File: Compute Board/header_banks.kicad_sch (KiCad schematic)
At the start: 12 parts, among them J3 Conn_01x02, J4 Conn_02x06_Top_Bottom, J5 Conn_02x08_Counter_Clockwise, J6 Conn_01x06, J7 Conn_01x07, J8 Conn_01x05, J9 Conn_01x08

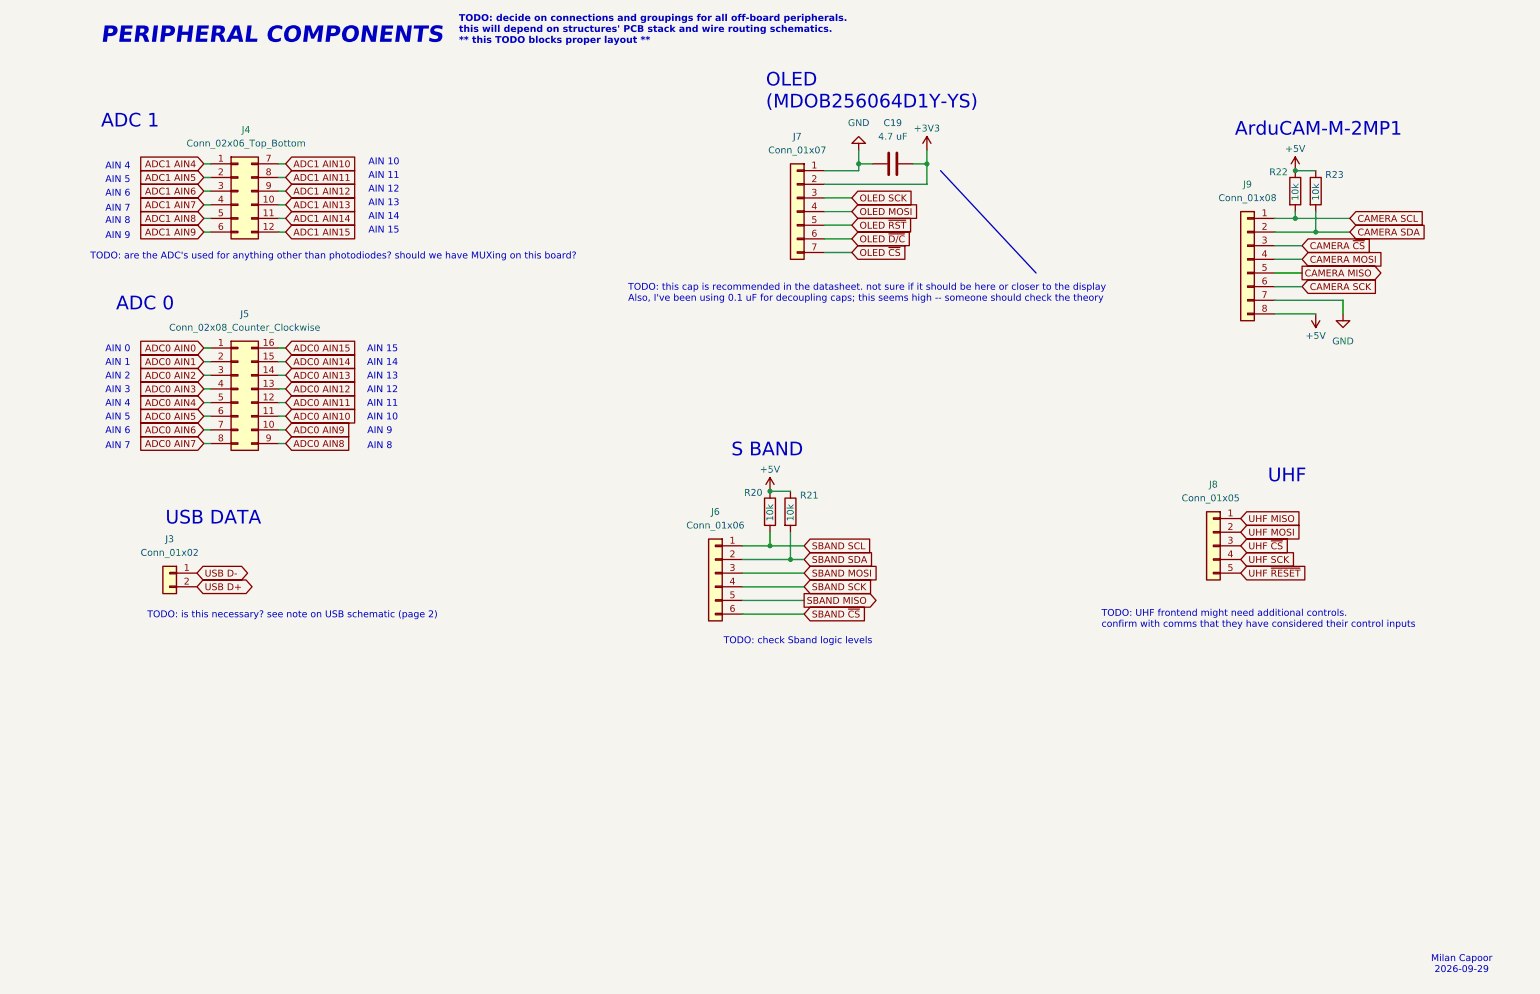
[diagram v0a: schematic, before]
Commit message: Push layout-ready schematics and partial routing
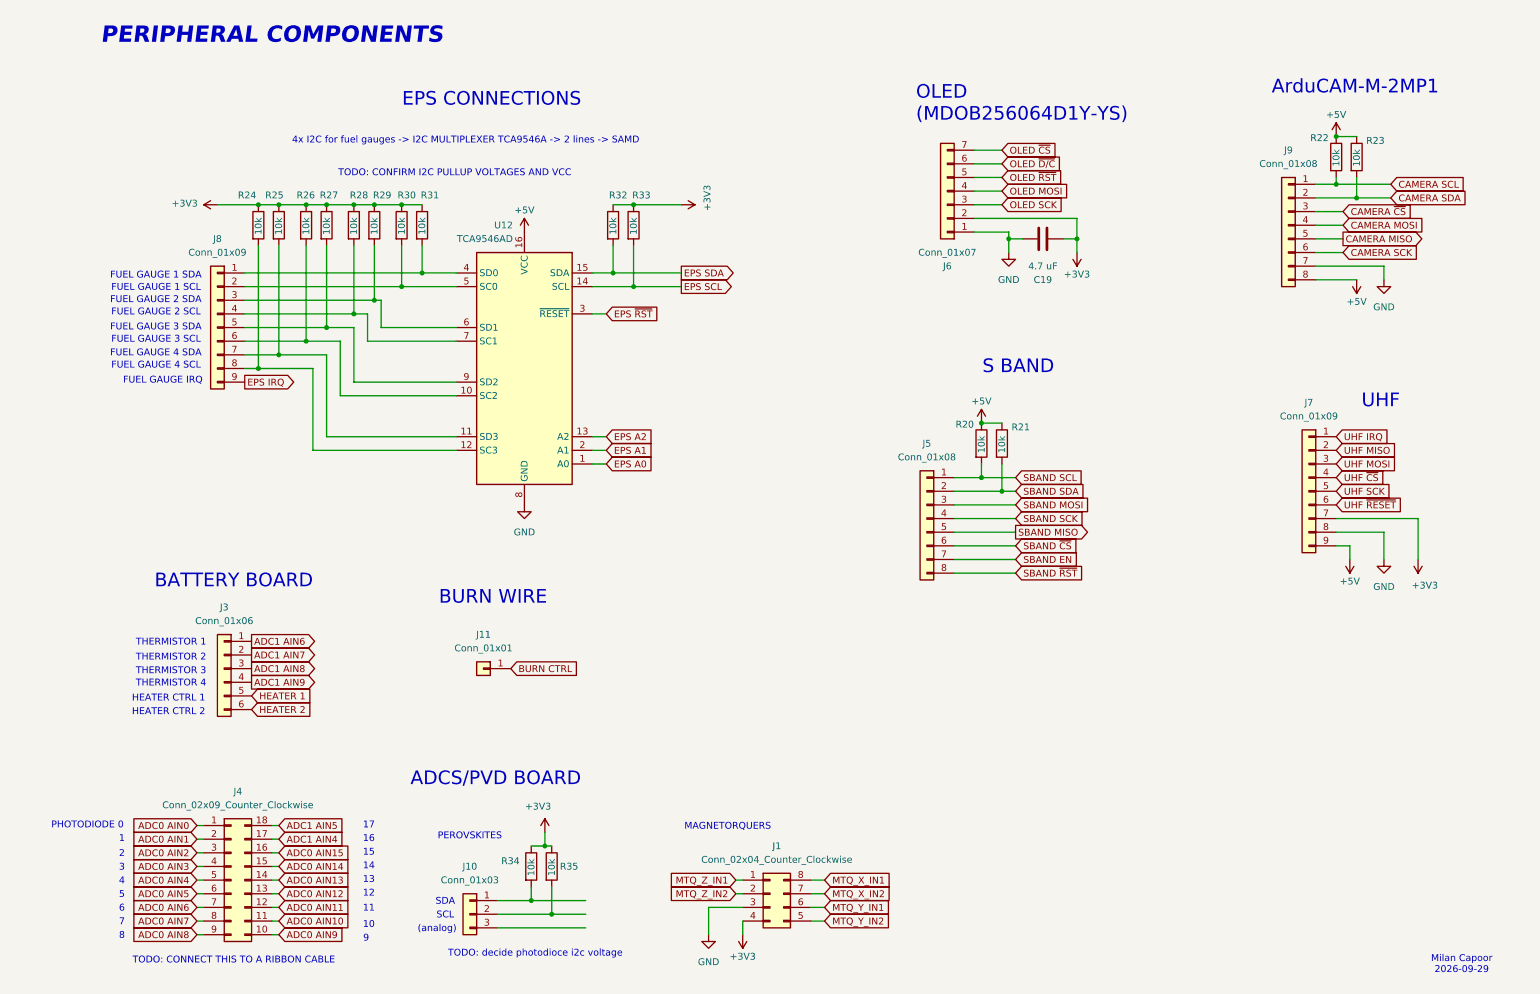
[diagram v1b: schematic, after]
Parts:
- removed J3: Conn_01x02, Connector_PinSocket_2.54mm:PinSocket_1x02_P2.54mm_Vertical, symbol Connector_Generic:Conn_01x02
- removed J4: Conn_02x06_Top_Bottom, Connector_PinSocket_2.54mm:PinSocket_2x06_P2.54mm_Vertical, symbol Connector_Generic:Conn_02x06_Top_Bottom
- removed J5: Conn_02x08_Counter_Clockwise, Connector_PinSocket_2.54mm:PinSocket_2x08_P2.54mm_Vertical, symbol Connector_Generic:Conn_02x08_Counter_Clockwise
- removed J6: Conn_01x06, Connector_PinSocket_2.54mm:PinSocket_1x06_P2.54mm_Vertical, symbol Connector_Generic:Conn_01x06
- removed J7: Conn_01x07, Connector_PinSocket_2.54mm:PinSocket_1x07_P2.54mm_Vertical, symbol Connector_Generic:Conn_01x07
- removed J8: Conn_01x05, Connector_PinSocket_2.54mm:PinSocket_1x05_P2.54mm_Vertical, symbol Connector_Generic:Conn_01x05
- added J1: Conn_02x04_Counter_Clockwise, Connector_PinSocket_2.54mm:PinSocket_2x04_P2.54mm_Vertical, symbol Connector_Generic:Conn_02x04_Counter_Clockwise
- added J10: Conn_01x03, Connector_PinSocket_2.54mm:PinSocket_1x03_P2.54mm_Vertical, symbol Connector_Generic:Conn_01x03
- added J11: Conn_01x01, Connector_PinSocket_2.54mm:PinSocket_1x01_P2.54mm_Vertical, symbol Connector_Generic:Conn_01x01
- added J3: Conn_01x06, Connector_PinSocket_2.54mm:PinSocket_1x06_P2.54mm_Vertical, symbol Connector_Generic:Conn_01x06
- added J4: Conn_02x09_Counter_Clockwise, symbol Connector_Generic:Conn_02x09_Counter_Clockwise
- added J5: Conn_01x08, Connector_PinSocket_2.54mm:PinSocket_1x08_P2.54mm_Vertical, symbol Connector_Generic:Conn_01x08
- added J6: Conn_01x07, Connector_PinSocket_2.54mm:PinSocket_1x07_P2.54mm_Vertical, symbol Connector_Generic:Conn_01x07
- added J7, J8: Conn_01x09, Connector_PinSocket_2.54mm:PinSocket_1x09_P2.54mm_Vertical, symbol Connector_Generic:Conn_01x09
- added R24, R25, R26, R27, R28, R29, R30, R31, R32, R33, R34, R35: 10k, Resistor_SMD:R_0603_1608Metric, symbol Device:R
- added U12: TCA9546AD, Package_SO:SOIC-16_3.9x9.9mm_P1.27mm, symbol Interface_Expansion:TCA9546AD
- C19: footprint Capacitor_SMD:C_0402_1005Metric -> Capacitor_SMD:C_0603_1608Metric
- R20, R21, R22, R23: footprint Resistor_SMD:R_0402_1005Metric -> Resistor_SMD:R_0603_1608Metric
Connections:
- net +3V3: now also J1.4 (Pin_4), J6.2 (Pin_2), J7.7 (Pin_7), R24.1, R25.1, R26.1, R27.1, R28.1, R29.1, R30.1, R31.1, R32.1, R33.1, R34.1, R35.1
- net +5V: now also J7.9 (Pin_9), U12.16 (VCC)
- net ADC0 AIN0: now also J4.1 (Pin_1)
- net ADC0 AIN1: now also J4.2 (Pin_2)
- net ADC0 AIN10: now also J4.11 (Pin_11)
- net ADC0 AIN11: now also J4.12 (Pin_12)
- net ADC0 AIN12: now also J4.13 (Pin_13)
- net ADC0 AIN13: now also J4.14 (Pin_14)
- net ADC0 AIN14: now also J4.15 (Pin_15)
- net ADC0 AIN15: now also J4.16 (Pin_16)
- net ADC0 AIN2: now also J4.3 (Pin_3)
- net ADC0 AIN3: now also J4.4 (Pin_4)
- net ADC0 AIN4: now also J4.5 (Pin_5)
- net ADC0 AIN5: now also J4.6 (Pin_6)
- net ADC0 AIN6: now also J4.7 (Pin_7)
- net ADC0 AIN7: now also J4.8 (Pin_8)
- net ADC0 AIN8: now also J4.9 (Pin_9)
- net ADC0 AIN9: now also J4.10 (Pin_10)
- net ADC1 AIN4: now also J4.17 (Pin_17)
- net ADC1 AIN5: now also J4.18 (Pin_18)
- net ADC1 AIN6: now also J3.1 (Pin_1)
- net ADC1 AIN7: now also J3.2 (Pin_2)
- net ADC1 AIN8: now also J3.3 (Pin_3)
- net ADC1 AIN9: now also J3.4 (Pin_4)
- net GND: now also J1.3 (Pin_3), J6.1 (Pin_1), J7.8 (Pin_8), U12.8 (GND)
- net OLED MOSI: now also J6.4 (Pin_4)
- net OLED SCK: now also J6.3 (Pin_3)
- net OLED ~{CS}: now also J6.7 (Pin_7)
- net OLED ~{D/C}: now also J6.6 (Pin_6)
- net OLED ~{RST}: now also J6.5 (Pin_5)
- net SBAND MISO: now also J5.5 (Pin_5)
- net SBAND MOSI: now also J5.3 (Pin_3)
- net SBAND SCK: now also J5.4 (Pin_4)
- net SBAND SCL: now also J5.1 (Pin_1)
- net SBAND SDA: now also J5.2 (Pin_2)
- net SBAND ~{CS}: now also J5.6 (Pin_6)
- net UHF MISO: now also J7.2 (Pin_2)
- net UHF MOSI: now also J7.3 (Pin_3)
- net UHF SCK: now also J7.5 (Pin_5)
- net UHF ~{CS}: now also J7.4 (Pin_4)
- net UHF ~{RESET}: now also J7.6 (Pin_6)
- new net: J8.7 (Pin_7), R25.2, U12.11 (SD3)
- new net: J8.4 (Pin_4), R28.2, U12.7 (SC1)
- new net: J8.1 (Pin_1), R31.2, U12.4 (SD0)
- new net: J8.2 (Pin_2), R30.2, U12.5 (SC0)
- new net: J8.3 (Pin_3), R29.2, U12.6 (SD1)
- new net: J8.5 (Pin_5), R27.2, U12.9 (SD2)
- new net: J8.6 (Pin_6), R26.2, U12.10 (SC2)
- new net: J8.8 (Pin_8), R24.2, U12.12 (SC3)
- new net: J10.2 (Pin_2), R35.2
- new net: J10.1 (Pin_1), R34.2
- new net BURN CTRL: J11.1 (Pin_1)
- new net EPS A0: U12.1 (A0)
- new net EPS A1: U12.2 (A1)
- new net EPS A2: U12.13 (A2)
- new net EPS IRQ: J8.9 (Pin_9)
- new net EPS SCL: R33.2, U12.14 (SCL)
- new net EPS SDA: R32.2, U12.15 (SDA)
- new net EPS ~{RST}: U12.3 (~{RESET})
- new net HEATER 1: J3.5 (Pin_5)
- new net HEATER 2: J3.6 (Pin_6)
- new net MTQ_X_IN1: J1.8 (Pin_8)
- new net MTQ_X_IN2: J1.7 (Pin_7)
- new net MTQ_Y_IN1: J1.6 (Pin_6)
- new net MTQ_Y_IN2: J1.5 (Pin_5)
- new net MTQ_Z_IN1: J1.1 (Pin_1)
- new net MTQ_Z_IN2: J1.2 (Pin_2)
- new net SBAND EN: J5.7 (Pin_7)
- new net SBAND ~{RST}: J5.8 (Pin_8)
- new net UHF IRQ: J7.1 (Pin_1)
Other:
- note added: "(analog)"
- note added: "1"
- note added: "10"
- note added: "11"
- note added: "12"
- note added: "13"
- note added: "14"
- note added: "15"
- note added: "16"
- note added: "17"
- note added: "2"
- note added: "3"
- note added: "4"
- note added: "4x I2C for fuel gauges -> I2C MULTIPLEXER TCA9546A -> 2 lines -> SAMD"
- note added: "5"
- note added: "6"
- note added: "7"
- note added: "8"
- note added: "9"
- note added: "ADCS/PVD BOARD"
- note added: "BATTERY BOARD"
- note added: "BURN WIRE"
- note added: "EPS CONNECTIONS"
- note added: "FUEL GAUGE 1 SCL"
- note added: "FUEL GAUGE 1 SDA"
- note added: "FUEL GAUGE 2 SCL"
- note added: "FUEL GAUGE 2 SDA"
- note added: "FUEL GAUGE 3 SCL"
- note added: "FUEL GAUGE 3 SDA"
- note added: "FUEL GAUGE 4 SCL"
- note added: "FUEL GAUGE 4 SDA"
- note added: "FUEL GAUGE IRQ"
- note added: "HEATER CTRL 1"
- note added: "HEATER CTRL 2"
- note added: "MAGNETORQUERS"
- note added: "PEROVSKITES"
- note added: "PHOTODIODE 0"
- note added: "SCL"
- note added: "SDA"
- note added: "THERMISTOR 1"
- note added: "THERMISTOR 2"
- note added: "THERMISTOR 3"
- note added: "THERMISTOR 4"
- note added: "TODO: CONFIRM I2C PULLUP VOLTAGES AND VCC"
- note added: "TODO: CONNECT THIS TO A RIBBON CABLE"
- note added: "TODO: decide photodioce i2c voltage"
- note removed: "ADC 0"
- note removed: "ADC 1"
- note removed: "AIN 0"
- note removed: "AIN 1"
- note removed: "AIN 10"
- note removed: "AIN 11"
- note removed: "AIN 12"
- note removed: "AIN 13"
- note removed: "AIN 14"
- note removed: "AIN 15"
- note removed: "AIN 2"
- note removed: "AIN 3"
- note removed: "AIN 4"
- note removed: "AIN 5"
- note removed: "AIN 6"
- note removed: "AIN 7"
- note removed: "AIN 8"
- note removed: "AIN 9"
- note removed: "TODO: UHF frontend might need additional controls. confirm with comms that they have considered their control inputs"
- note removed: "TODO: are the ADC's used for anything other than photodiodes? should we have MUXing on this board?"
- note removed: "TODO: check Sband logic levels"
- note removed: "TODO: decide on connections and groupings for all off-board peripherals. this will depend on structures' PCB stack and wire routing schematics. ** this TODO blocks proper layout **"
- note removed: "TODO: is this necessary? see note on USB schematic (page 2)"
- note removed: "TODO: this cap is recommended in the datasheet. not sure if it should be here or closer to the display Also, I've been using 0.1 uF for decoupling caps; this seems high -- someone should check the theory"
- note removed: "USB DATA"
- moved on the sheet: C19, J9, R20, R21, R22, R23

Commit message: Push finished layout minus perovskites
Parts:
- removed J4: Conn_02x09_Counter_Clockwise, symbol Connector_Generic:Conn_02x09_Counter_Clockwise
- added J13: Conn_01x18, Ribbon cables:FH34SRJ18S05SH50, symbol Connector_Generic:Conn_01x18
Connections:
- net ADC0 AIN0: now also J13.1 (Pin_1)
- net ADC0 AIN1: now also J13.2 (Pin_2)
- net ADC0 AIN10: now also J13.11 (Pin_11)
- net ADC0 AIN11: now also J13.12 (Pin_12)
- net ADC0 AIN12: now also J13.13 (Pin_13)
- net ADC0 AIN13: now also J13.14 (Pin_14)
- net ADC0 AIN14: now also J13.15 (Pin_15)
- net ADC0 AIN15: now also J13.16 (Pin_16)
- net ADC0 AIN2: now also J13.3 (Pin_3)
- net ADC0 AIN3: now also J13.4 (Pin_4)
- net ADC0 AIN4: now also J13.5 (Pin_5)
- net ADC0 AIN5: now also J13.6 (Pin_6)
- net ADC0 AIN6: now also J13.7 (Pin_7)
- net ADC0 AIN7: now also J13.8 (Pin_8)
- net ADC0 AIN8: now also J13.9 (Pin_9)
- net ADC0 AIN9: now also J13.10 (Pin_10)
- net ADC1 AIN4: now also J13.17 (Pin_17)
- net ADC1 AIN5: now also J13.18 (Pin_18)
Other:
- note added: "DAC"
- note added: "TODO: confirm photodioce i2c voltage and that this is all circuitry needed"
- note removed: "(analog)"
- note removed: "TODO: CONNECT THIS TO A RIBBON CABLE"
- note removed: "TODO: decide photodioce i2c voltage"
- moved on the sheet: J3

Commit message: Add perovskite and magnetorquer sleep routing
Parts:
- removed J1: Conn_02x04_Counter_Clockwise, Connector_PinSocket_2.54mm:PinSocket_2x04_P2.54mm_Vertical, symbol Connector_Generic:Conn_02x04_Counter_Clockwise
- added J4: Conn_02x06_Counter_Clockwise, Connector_PinSocket_2.54mm:PinSocket_2x06_P2.54mm_Vertical, symbol Connector_Generic:Conn_02x06_Counter_Clockwise
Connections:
- net CAMERA SCL is gone; now on net CAMERA/PVD SCL: J9.1 (Pin_1), R22.2
- net CAMERA SDA is gone; now on net CAMERA/PVD SDA: J9.2 (Pin_2), R23.2
- net +3V3: now also J4.6 (Pin_6)
- net GND: now also J4.5 (Pin_5)
- net MTQ_X_IN1: now also J4.12 (Pin_12)
- net MTQ_X_IN2: now also J4.11 (Pin_11)
- net MTQ_Y_IN1: now also J4.10 (Pin_10)
- net MTQ_Y_IN2: now also J4.9 (Pin_9)
- net MTQ_Z_IN1: now also J4.1 (Pin_1)
- net MTQ_Z_IN2: now also J4.2 (Pin_2)
- net CAMERA/PVD SDA: now reaches J10.2 (Pin_2), R35.2
- net CAMERA/PVD SCL: now reaches J10.1 (Pin_1), R34.2
- net PVD DAC: now reaches J10.3 (Pin_3)
- new net MTQ_X_SLP: J4.3 (Pin_3)
- new net MTQ_Y_SLP: J4.8 (Pin_8)
- new net MTQ_Z_SLP: J4.7 (Pin_7)
- no-connect marks 0 -> 1
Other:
- note added: "TODO: EPS I2C NOT ROUTED"
- moved on the sheet: R34, R35

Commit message: Finished routing
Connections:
- net EPS SCL is gone; now on net CAMERA/PVD/EPS SDA: R33.2, U12.14 (SCL)
- net EPS SDA is gone; now on net CAMERA/PVD/EPS SCL: R32.2, U12.15 (SDA)
- net CAMERA/PVD SCL renamed CAMERA/PVD/EPS SCL
- net CAMERA/PVD SDA renamed CAMERA/PVD/EPS SDA
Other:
- note removed: "TODO: EPS I2C NOT ROUTED"
- moved on the sheet: J10, J9, R22, R23, R34, R35
